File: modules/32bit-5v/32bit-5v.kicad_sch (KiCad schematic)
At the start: 65 parts, among them J5 USB_C_Receptacle_USB2.0_14P, SW1 K2-1808SN-A4SW-01, SW2 K2-1808SN-A4SW-01, SW4 K2-1808SN-A4SW-01, U1 ESP32-S3-WROOM-1U-N16R8, U3 MCP6002-xSN, U5 AP7361C-33E-13

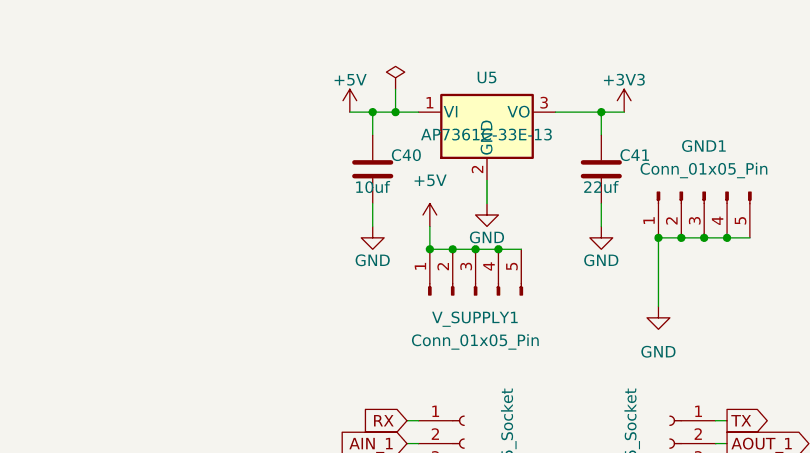
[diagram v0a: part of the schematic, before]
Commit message: 32bit-5v: 1.1.1 - swap the 3.3V regulator to the base's AP2112K-3.3 (schematic only)
Requested by the owner: "For 32bit, use the same regulator we use for the base
module for 3.3V conversion. It's small as well. You only do the schematics. I
will do the routing. We need to keep components in a single side."

* U5: AP7361C-33E-13 (SOT-223, C500795) -> AP2112K-3.3 (SOT-23-5, LCSC C51118,
  MPN AP2112K-3.3TRG1, Diodes, 600mA). Value/Footprint/Datasheet/Description/
  LCSC/MPN/Manufacturer copied verbatim from modules/base U5, so both boards
  order the identical part (machine-checked against the base schematic).
* EN tied directly to VIN (+5V): the module must always be on. The base's
  R4 100k + C16 220nF + SW1 enable network is deliberately not reproduced.
* New C42 = 0.1uF/16V X7R 0402, LCSC C1525 / CL05B104KO5NNNC - the base's own
  0.1uF part, as the regulator input HF cap (mirrors base C1/C21).
* C40 (10uF 0805, C15850) and C41 (22uF 0805, C45783) kept: same Samsung CL21
  0805 family as the base's caps, values left larger than the base's 1uF/4.7uF
  because the 5V arrives on the slot socket with no upstream bulk and the load is
  the ESP32 + ES8388, not the base's few mA.
* Net effect: +5V = {V_SUPPLY1.1-5, U5.VIN(1), U5.EN(3), C40.1, C42.1} and
  nothing else; +3V3 keeps every 1.1.0 load (only the regulator pin moved from
  VO 3 to VOUT 5); +3V3_ESP32 / +3V3_8388 unchanged; AP7361C gone everywhere.
* ERC (KiCad 10.0.6): 54 -> 54 findings (34 error / 20 warning), no new finding
  and no new finding kind.
* PCB deliberately untouched - no placement, no routing, no zone refill, no
  footprint deletion. pcb drc --schematic-parity therefore now reports the U5
  mismatch: expected and owned by the owner's routing pass. production/ BOM+CPL
  are left stale for the same reason (they come from the board via the JLCPCB
  toolkit; regenerate after routing).
* Headroom (owner-confirmed: WiFi/BT is never used): ~0.08-0.12A typical,
  ~0.15-0.2A peak -> the 600mA part has ~3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
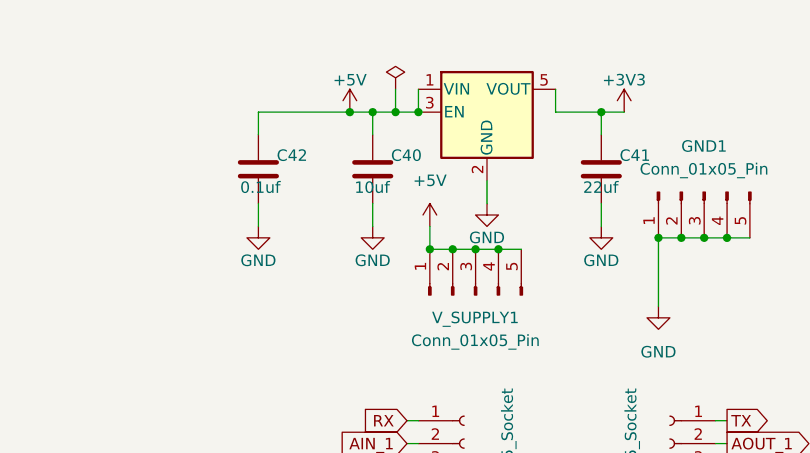
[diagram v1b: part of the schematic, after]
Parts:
- added C42: 0.1uf, Capacitor_SMD:C_0402_1005Metric, symbol Device:C
- U5: value AP7361C-33E-13 -> AP2112K-3.3; footprint Package_TO_SOT_SMD:SOT-223-3_TabPin2 -> Package_TO_SOT_SMD:SOT-23-5; symbol Regulator_Linear:AP7361C-33E -> Regulator_Linear:AP2112K-3.3; LCSC C500795 -> C51118; MPN AP7361C-33E-13 -> AP2112K-3.3TRG1; Manufacturer Diodes Incorporated -> Diodes
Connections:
- net +3V3: now also U5.5 (VOUT); no longer U5.3 (VO)
- net +5V: now also U5.3 (EN), C42.1
- net GND: now also C42.2

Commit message: Update the 32bit schematics a bit
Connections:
- net +3V3: no longer C41.1
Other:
- moved on the sheet: C40, C41, C42, V_SUPPLY1

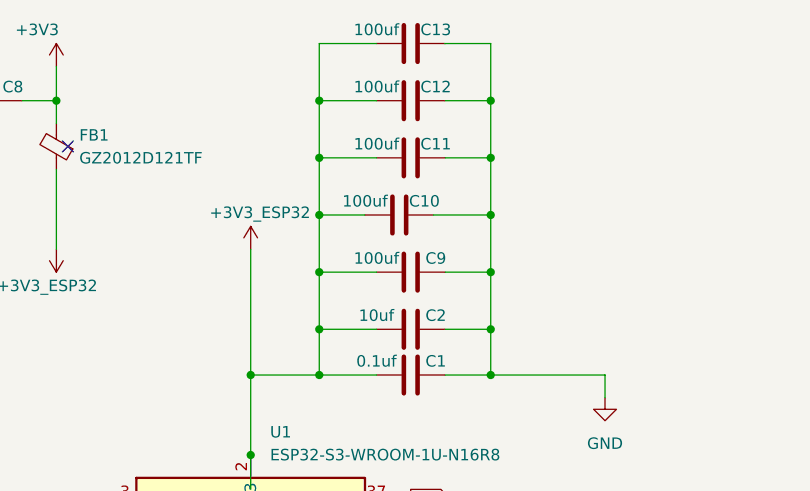
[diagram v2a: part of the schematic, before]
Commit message: 32bit-5v: v1.1.2 - trim ESP32 rail bulk (C9-C13 100uF removed per Espressif guidance), POWER.md/CHANGELOG/verification regenerated (netlist 20/20 + 19/19, ERC normalised identical to 1.1.1)
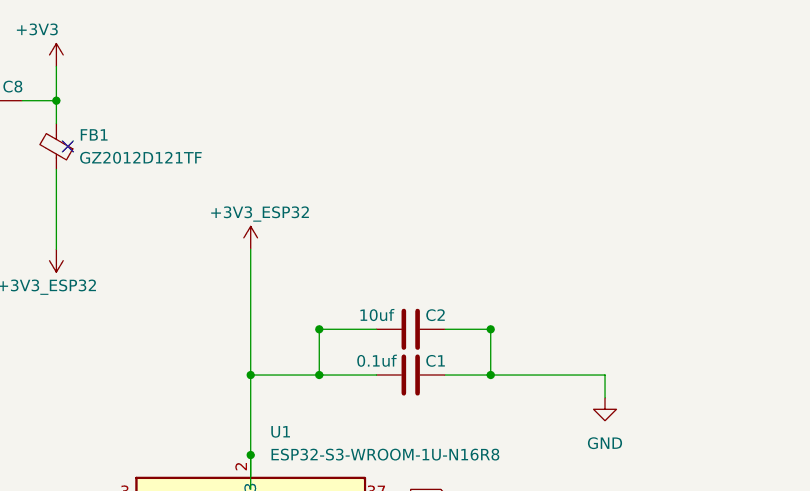
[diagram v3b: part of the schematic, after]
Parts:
- removed C10, C11, C12, C13, C9: 100uf, Capacitor_SMD:C_1206_3216Metric, symbol Device:C

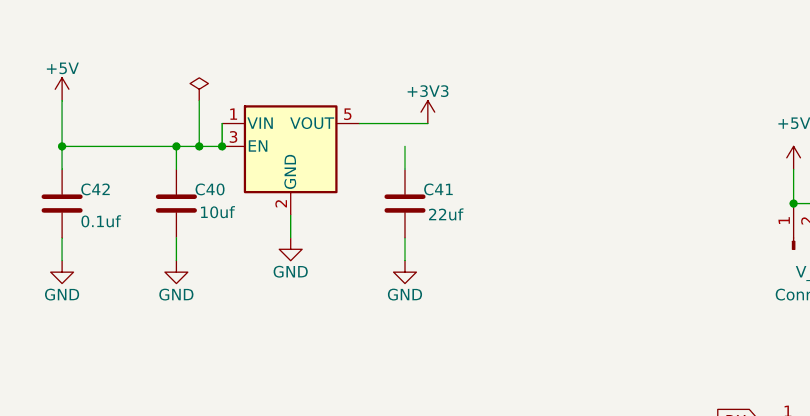
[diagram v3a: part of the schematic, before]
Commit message: 32bit-5v: v1.1.3 - fix C41 (22uF LDO output bulk): its +3V3 connection was missing since 1244ad0, one wire + junction added in the schematic; ERC 56 -> 54 (element-for-element the shipped 1.1.1 report), schematic parity 19 -> 18, board byte-identical
Schematic-only. C41's top stub wire (464.82, 29.21)->(464.82, 26.67) was left
ending in mid-air by 1244ad0 (the +3V3 run at y=24.13 passes 2.54mm above it), so
the netlist carried the auto net unconnected-(C41-Pad1) and ERC carried
+1 error pin_not_connected (C41 pin 1) +1 warning unconnected_wire_endpoint.

The board was never broken: C41.1 is +3V3 on B.Cu, reached by the 0.8mm track
(64.05,60.4)->(66.8,60.4), DRC reports 0 unconnected items both before and after,
and there is no +3V3 pour on this board - so no copper was added or removed.

Fix = the remedy scoped in POWER.md 5: wire (464.82,26.67)->(464.82,24.13) plus a
junction at (464.82,24.13). 16 added lines, 0 deleted, nothing moved.

Verified before -> after (KiCad 10.0.6 kicad-cli):
  netlist    77 -> 76 nets; unconnected-(C41-Pad1) gone; +3V3 gains exactly C41.1
             (9 -> 10 nodes) and is the only net whose node set changed
  sch erc    56 (35/21) -> 54 (34/20); normalised diff = exactly the two C41
             findings removed, none added (= the report shipped with v1.1.1)
  pcb drc    105 violations / 0 unconnected before and after (board untouched);
             --schematic-parity 19 -> 18, the removed item being exactly
             "Pad net (+3V3) doesn't match net given by schematic (unconnected-(C41-Pad1))"

Not touched: 32bit-5v.kicad_pcb (byte-identical, sha256 0294006d...), .kicad_pro,
production/, code/ and the verification/ fixture set (those are the 1.1.2 side of
the frozen 20/20 trim proof; regenerating them would invalidate it).
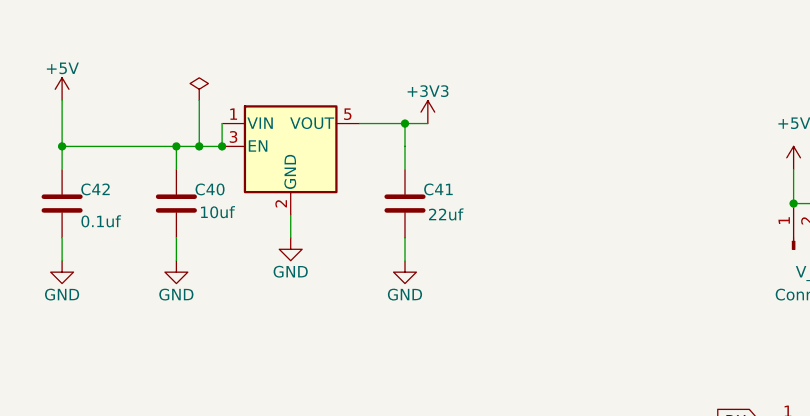
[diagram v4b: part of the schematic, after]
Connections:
- net +3V3: now also C41.1
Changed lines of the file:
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@@
+		(color 0 0 0 0)
+	)
+	(junction
+		(at 464.82 24.13)
+		(diameter 0)
 		(color 0 0 0 0)
 	)
@@
 		)
 		(stroke
+			(width 0)
+			(type default)
+		)
+	)
+	(wire
+		(pts
+			(xy 464.82 26.67) (xy 464.82 24.13)
+		)
+		(stroke

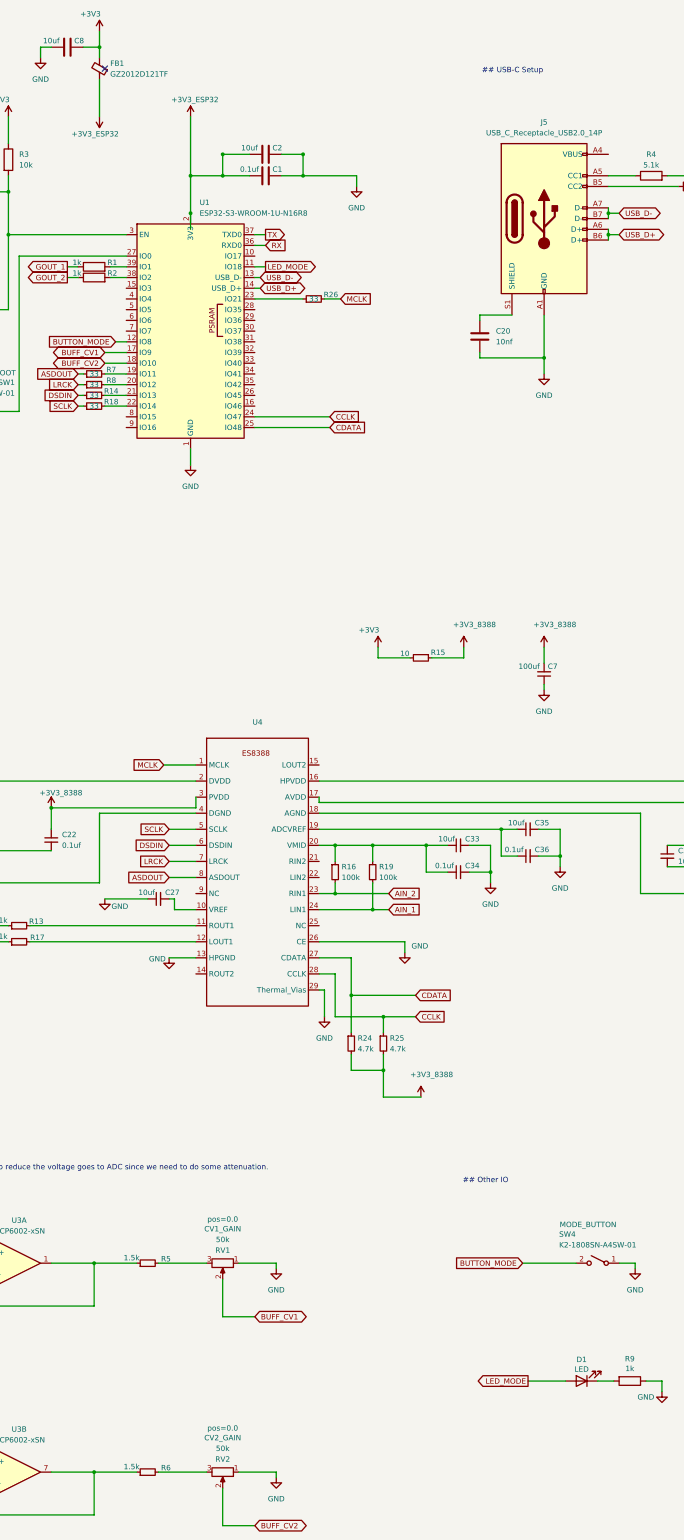
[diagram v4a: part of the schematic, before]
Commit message: Finish 32-bit 5V multilayer routing and exports; retain approved THT placement
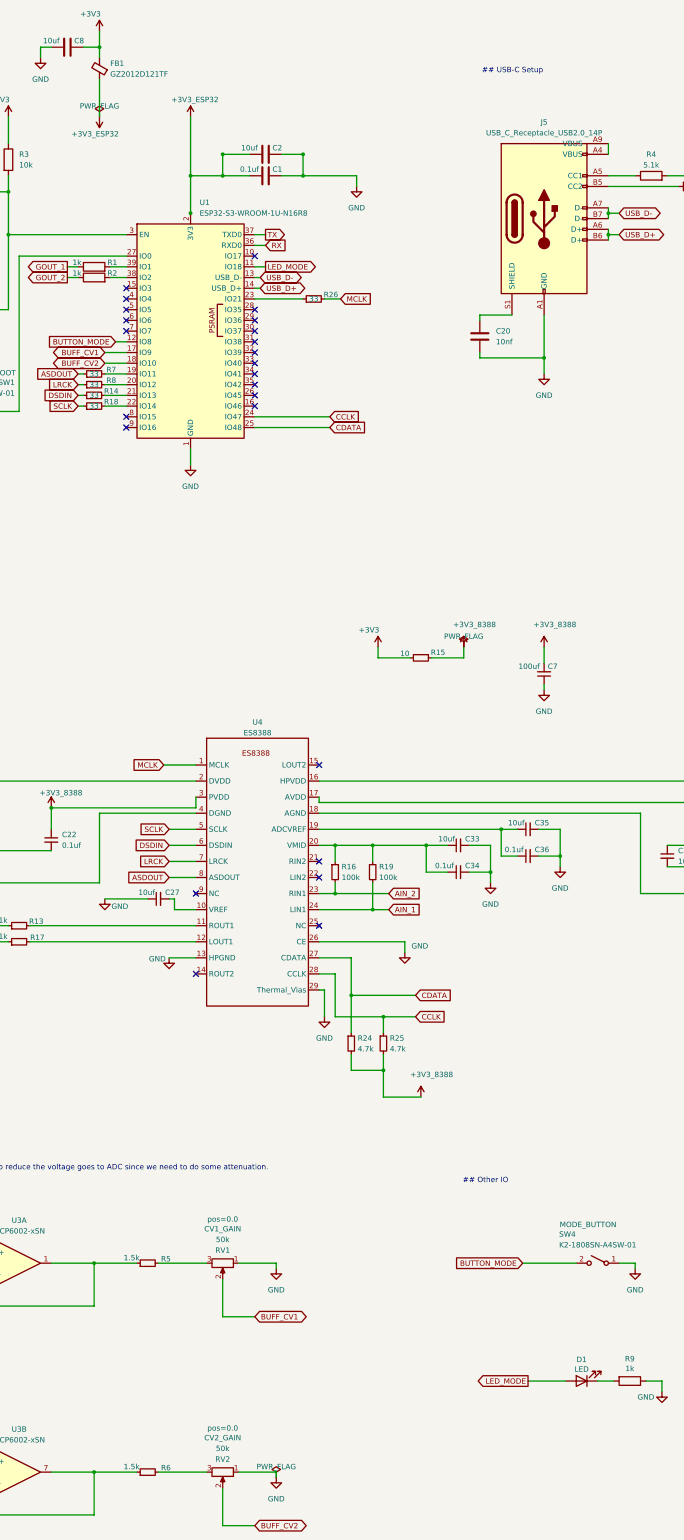
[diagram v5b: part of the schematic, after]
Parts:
- J5: footprint BreadModular_TypeC:HRO-TYPE-C-31-M-12 -> Module32:HRO-TYPE-C-31-M-12; symbol Connector:USB_C_Receptacle_USB2.0_14P -> Module32:HRO_TYPE_C_31_M_12
- U3: footprint Package_SO:SOIC-8-1EP_3.9x4.9mm_P1.27mm_EP2.29x3mm -> Package_SO:SOIC-8_3.9x4.9mm_P1.27mm
- U4: value (none) -> ES8388; footprint Package_DFN_QFN:QFN-28-1EP_4x4mm_P0.45mm_EP2.4x2.4mm_ThermalVias -> Module32:ES8388_QFN28_4x4_P0.45_EP2.6_ThermalVias; symbol BreadModular_Symbols:ES8388 -> Module32:ES8388; MPN (none) -> ES8388; Manufacturer (none) -> Everest Semiconductor
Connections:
- net GND: no longer J5.B1 (GND), J5.B12 (GND)
- net at J5.A4 (VBUS), J5.A9 (VBUS): no longer J5.B4 (VBUS), J5.B9 (VBUS)
- no-connect marks 1 -> 24
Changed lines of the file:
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@@
 		(color 0 0 0 0)
 	)
-	(no_connect
-		(at 76.2 26.67)
-	)
 	(wire
 		(pts
@@
 	(wire
 		(pts
-			(xy 96.52 64.77) (xy 96.52 60.96)
-		)
-		(stroke
-			(width 0)
-			(type default)
-		)
-	)
-	(wire
-		(pts
 			(xy 76.2 93.98) (xy 81.28 93.98)
 		)
@@
 			)
 		)
-		(property "Footprint" "Package_SO:SOIC-8-1EP_3.9x4.9mm_P1.27mm_EP2.29x3mm"
+		(property "Footprint" "Package_SO:SOIC-8_3.9x4.9mm_P1.27mm"
 			(at 55.88 309.88 0)
 			(hide yes)
@@
 	)
 	(symbol
-		(lib_id "Connector:USB_C_Receptacle_USB2.0_14P")
+		(lib_id "Module32:HRO_TYPE_C_31_M_12")
 		(at 180.34 62.23 0)
 		(unit 1)
@@
 			)
 		)
-		(property "Footprint" "BreadModular_TypeC:HRO-TYPE-C-31-M-12"
+		(property "Footprint" "Module32:HRO-TYPE-C-31-M-12"
 			(at 184.15 62.23 0)
 			(hide yes)
@@
 		(pin "B7"
 		)
-		(pin "B9"
-		)
 		(pin "B5"
 		)
@@
 		(pin "A6"
 		)
-		(pin "B12"
-		)
-		(pin "B4"
-		)
 		(pin "A1"
 		)
@@
 		(pin "A9"
 		)
-		(pin "B1"
-		)
 		(pin "S1"
 		)
@@
 			)
 		)
-		(property "Footprint" "Package_SO:SOIC-8-1EP_3.9x4.9mm_P1.27mm_EP2.29x3mm"
+		(property "Footprint" "Package_SO:SOIC-8_3.9x4.9mm_P1.27mm"
 			(at 523.24 132.08 0)
 			(hide yes)
@@
 			)
 		)
-		(property "Footprint" "Package_SO:SOIC-8-1EP_3.9x4.9mm_P1.27mm_EP2.29x3mm"
+		(property "Footprint" "Package_SO:SOIC-8_3.9x4.9mm_P1.27mm"
 			(at 55.88 359.41 0)
 			(hide yes)
@@
 	)
 	(symbol
-		(lib_id "BreadModular_Symbols:ES8388")
+		(lib_id "Module32:ES8388")
 		(at 111.76 209.55 0)
 		(unit 1)
@@
 			)
 		)
-		(property "Value" ""
+		(property "Value" "ES8388"
 			(at 112.395 184.15 0)
 			(show_name no)
@@
 			)
 		)
-		(property "Footprint" "Package_DFN_QFN:QFN-28-1EP_4x4mm_P0.45mm_EP2.4x2.4mm_ThermalVias"
+		(property "Footprint" "Module32:ES8388_QFN28_4x4_P0.45_EP2.6_ThermalVias"
 			(at 111.76 209.55 0)
 			(hide yes)
@@
 			)
 		)
-		(property "Datasheet" ""
+		(property "Datasheet" "https://www.lcsc.com/datasheet/lcsc_datasheet_2410121449_Everest-semi-Everest-Semiconductor-ES8388_C365736.pdf"
 			(at 111.76 209.55 0)
 			(hide yes)
@@
 			)
 		)
-		(property "Description" ""
+		(property "Description" "ES8388 low-power stereo audio CODEC with headphone amplifier; QFN-28; existing exposed-pad/thermal-via footprint retained"
+			(at 111.76 209.55 0)
+			(hide yes)
+			(show_name no)
+			(do_not_autoplace no)
+			(effects
+				(font
+					(size 1.27 1.27)
+				)
+			)
+		)
+		(property "MPN" "ES8388"
+			(at 111.76 209.55 0)
+			(hide yes)
+			(show_name no)
+			(do_not_autoplace no)
+			(effects
+				(font
+					(size 1.27 1.27)
+				)
+			)
+		)
+		(property "Manufacturer" "Everest Semiconductor"
 			(at 111.76 209.55 0)
 			(hide yes)
@@
 	)
 	(embedded_fonts no)
+(no_connect (at 81.28 81.28))
+(no_connect (at 81.28 83.82))
+(no_connect (at 81.28 86.36))
+(no_connect (at 81.28 88.9))
+(no_connect (at 81.28 109.22))
+(no_connect (at 81.28 111.76))
+(no_connect (at 111.76 71.12))
+(no_connect (at 81.28 78.74))
+(no_connect (at 111.76 106.68))
+(no_connect (at 111.76 104.14))
+(no_connect (at 111.76 83.82))
+(no_connect (at 111.76 86.36))
+(no_connect (at 111.76 88.9))
+(no_connect (at 111.76 91.44))
+(no_connect (at 111.76 93.98))
+(no_connect (at 111.76 96.52))
+(no_connect (at 111.76 99.06))
+(no_connect (at 111.76 101.6))
+(no_connect (at 97.79 222.25))
+(no_connect (at 97.79 241.3))
+(no_connect (at 127.0 191.77))
+(no_connect (at 127.0 214.63))
+(no_connect (at 127.0 218.44))
+(no_connect (at 127.0 229.87))
+(symbol (lib_id "power:PWR_FLAG") (at 74.93 38.1 0) (unit 1)
+      (in_bom no) (on_board yes) (dnp no)
+      (property "Reference" "#FLG03201" (at 74.93 38.1 0) (effects (font (size 1.27 1.27)) (hide yes)))
+      (property "Value" "PWR_FLAG" (at 74.93 35.56 0) (effects (font (size 1.27 1.27))))
+      (pin "1")
+      (instances (project "32bit-5v" (path "/b63493d3-5f6d-47e3-845b-87e7090fc1ab" (reference "#FLG03201") (unit 1)))))
+(symbol (lib_id "power:PWR_FLAG") (at 161.29 163.83 0) (unit 1)
+      (in_bom no) (on_board yes) (dnp no)
+      (property "Reference" "#FLG03202" (at 161.29 163.83 0) (effects (font (size 1.27 1.27)) (hide yes)))
+      (property "Value" "PWR_FLAG" (at 161.29 161.29000000000002 0) (effects (font (size 1.27 1.27))))
+      (pin "1")
+      (instances (project "32bit-5v" (path "/b63493d3-5f6d-47e3-845b-87e7090fc1ab" (reference "#FLG03202") (unit 1)))))
+(symbol (lib_id "power:PWR_FLAG") (at 116.84 360.68 0) (unit 1)
+      (in_bom no) (on_board yes) (dnp no)
+      (property "Reference" "#FLG03203" (at 116.84 360.68 0) (effects (font (size 1.27 1.27)) (hide yes)))
+      (property "Value" "PWR_FLAG" (at 116.84 358.14 0) (effects (font (size 1.27 1.27))))
+      (pin "1")
+      (instances (project "32bit-5v" (path "/b63493d3-5f6d-47e3-845b-87e7090fc1ab" (reference "#FLG03203") (unit 1)))))
+(wire (pts (xy 195.58 46.99) (xy 195.58 44.45)) (stroke (width 0) (type default)))
 )
